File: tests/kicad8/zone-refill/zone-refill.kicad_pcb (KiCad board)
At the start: 2 copper layers, 15 x 8 mm, 4 parts, among them J1 Conn_01x02_Male, J2 Conn_01x02_Male

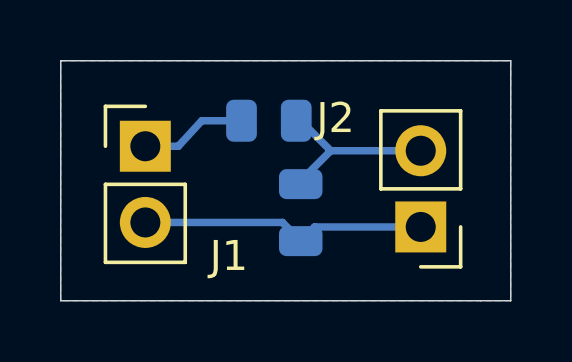
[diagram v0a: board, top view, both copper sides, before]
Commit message: [PCBNew][DRC] Implemented CLI version
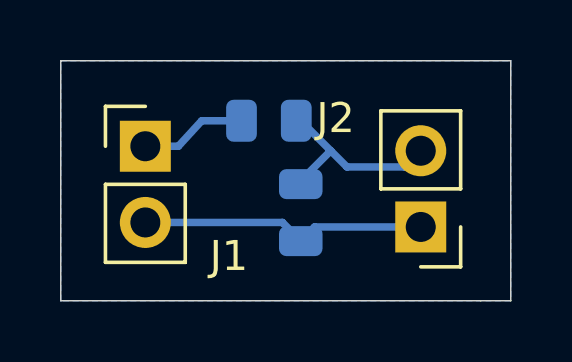
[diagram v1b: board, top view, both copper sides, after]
